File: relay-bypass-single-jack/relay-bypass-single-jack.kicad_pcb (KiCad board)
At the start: 2 copper layers, 59 x 25.8 mm, 62 parts, among them J1 4, J2 8, J3 4, J4 3, K1 IM05JR, Q1 DMN62D0U-7, Q2 DMP3099L, Q3 DMN62D0U-7, U1 STM32C011F4Ux, U3 TLV76701DRVR, U6 TLP170AM

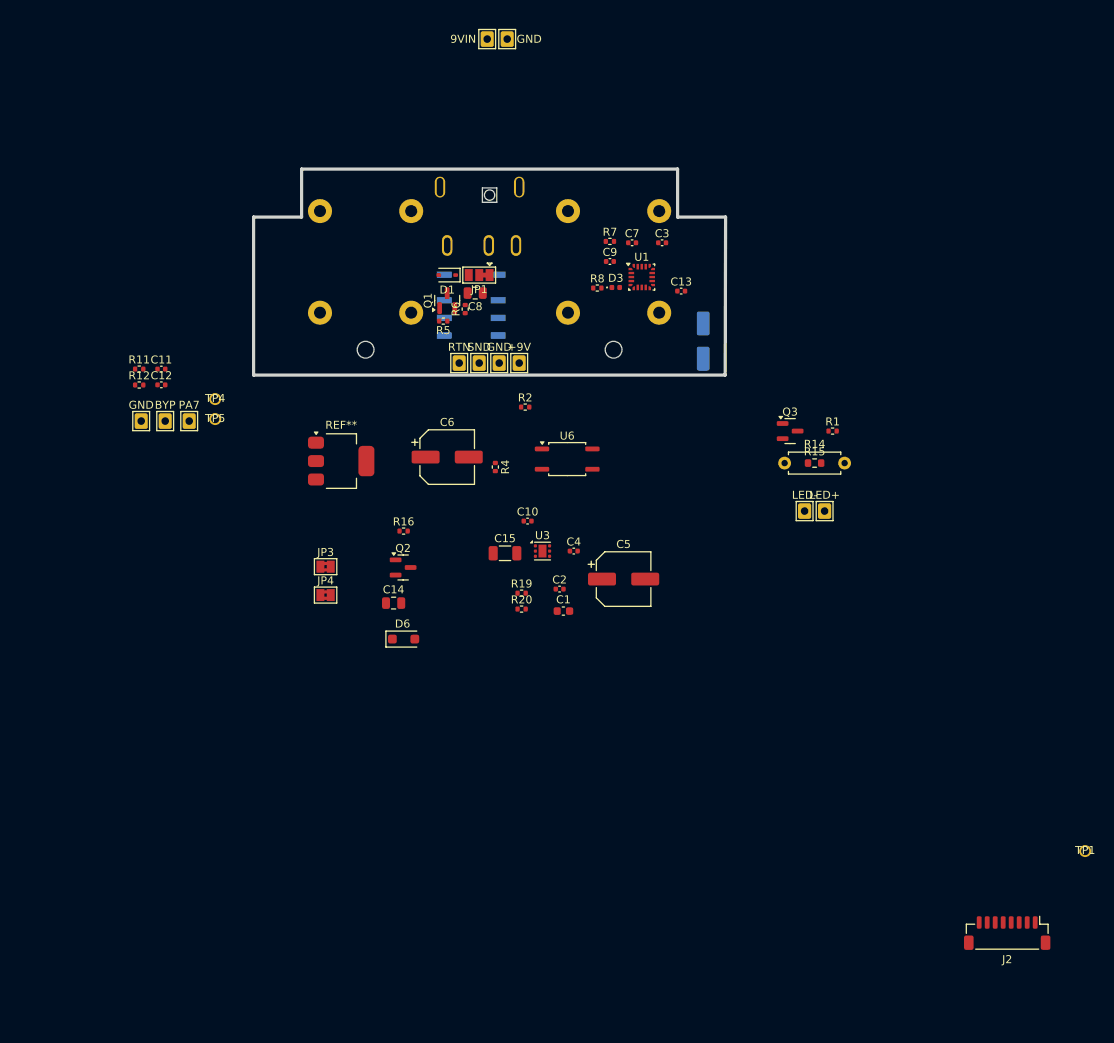
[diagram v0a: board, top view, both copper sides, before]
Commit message: Added second project for exploring a single-jack side mounted version
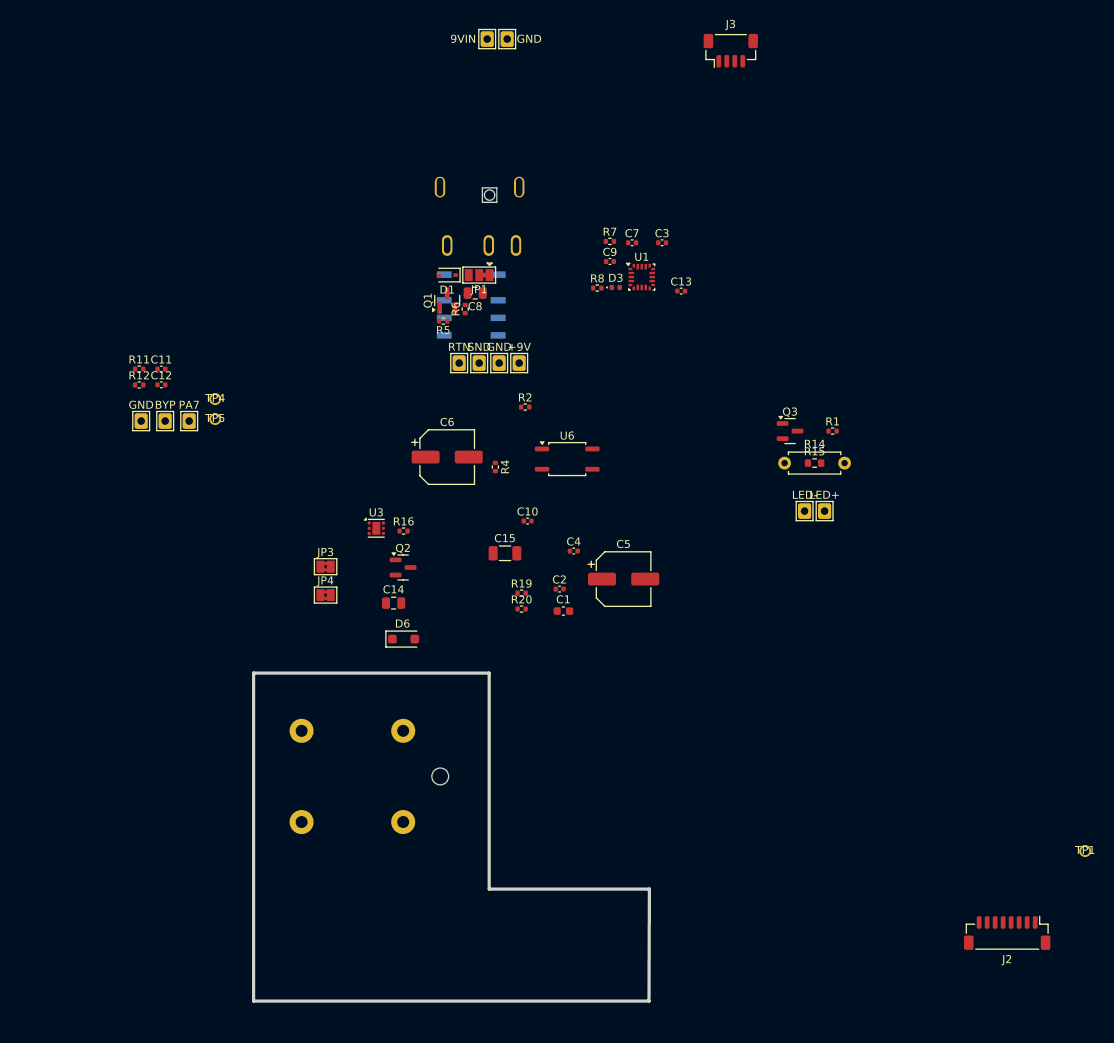
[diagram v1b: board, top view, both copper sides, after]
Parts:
- removed REF**: SOT-223, Package_TO_SOT_SMD:SOT-223
- removed REF**: CP_Elec_5x5.8, Capacitor_SMD:CP_Elec_5x5.8
- J3: footprint g-con:Amphenol_ACJM-MHDR(M) -> Connector_JST:JST_SH_BM04B-SRSS-TB_1x04-1MP_P1.00mm_Vertical; moved to F.Cu
- moved J1 75.9 mm to (72.3, 126.9), turned to 180 degrees
- moved J3 21.5 mm to (130.2, 36.2), turned to 0 degrees
- moved U3 21.0 mm to (85.9, 95.9)
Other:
- board size 59 x 25.8 mm -> 49.5 x 41 mm
- board text added: "TODO add 1590b enclosure dimensions"

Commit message: Pivoted to dual-jack version on opposing sides.
125B only, using "innie" jacks. Solder-in-place.
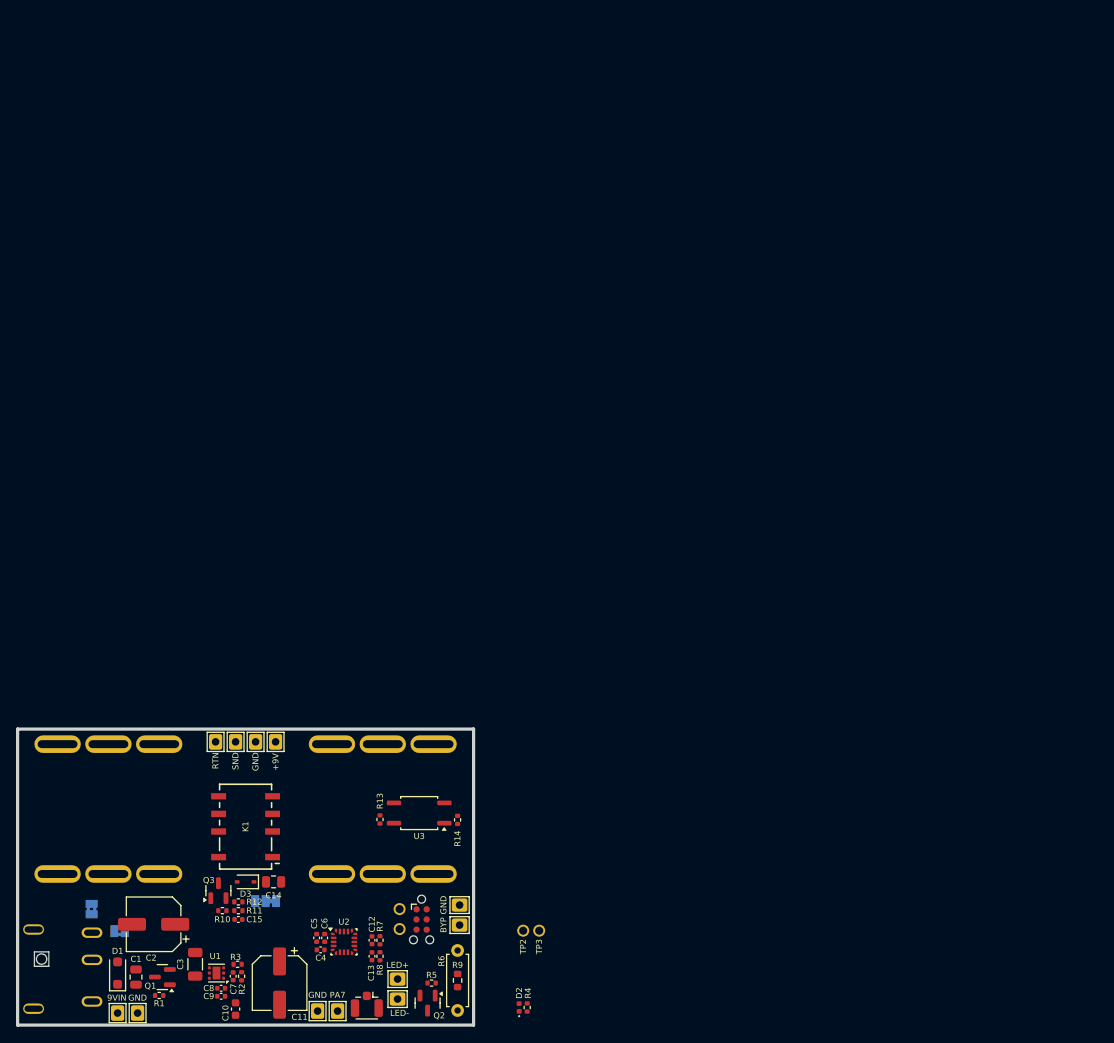
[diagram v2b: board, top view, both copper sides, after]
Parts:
- removed the J1 at (72.3, 126.9)
- removed TP1: PA3, g-art:TestPoint_PTH_H1.02mm_NoOutline
- added J4: AudioJack3_Switch, g-con:Jack_6.35mm_Neutrik_NMJ6HCD2_LARGE_SLOTS, B.Cu at (100.0, 131.0)
- added J5: Conn_Coaxial_Small, Connector_Coaxial:U.FL_Hirose_U.FL-R-SMT-1_Vertical, F.Cu at (84.7, 155.4)
- added REF**: Footswitch_SPST, g-art:Footswitch_SPST, F.Cu at (69.5, 153.5)
- added TP4: TX, g-art:TestPoint_PTH_H1.02mm_NoOutline, F.Cu at (88.8, 146.0)
- added TP5: RX, g-art:TestPoint_PTH_H1.02mm_NoOutline, F.Cu at (88.8, 143.5)
- added WP12: GND, g-art:WirePad_H0.95mm_22-24AWG, F.Cu at (78.5, 156.2)
- J2: value 8 -> TC2030; footprint Connector_JST:JST_SH_BM08B-SRSS-TB_1x08-1MP_P1.00mm_Vertical -> Connector:Tag-Connect_TC2030-IDC-NL_2x03_P1.27mm_Vertical
- J3: value 4 -> AudioJack3_Switch; footprint Connector_JST:JST_SH_BM04B-SRSS-TB_1x04-1MP_P1.00mm_Vertical -> g-con:Jack_6.35mm_Neutrik_NMJ6HCD2_LARGE_SLOTS; moved to B.Cu
- JP1: renamed from JP3; moved to B.Cu
- JP2: renamed from JP4; moved to B.Cu
- JP3: renamed from JP1; moved to B.Cu
- K1: moved to F.Cu
- moved J3 131.5 mm to (39.0, 131.0)
- moved WP1 130.2 mm to (53.5, 156.5)
- moved WP2 130.2 mm to (56.0, 156.5)
- moved J1 108.8 mm to (45.8, 151.0), turned to 180 degrees
- moved C6 96.6 mm to (79.4, 147.1), turned to -90 degrees
- moved R11 95.7 mm to (68.7, 143.7), turned to 180 degrees
- moved C5 95.4 mm to (78.4, 147.1), turned to -90 degrees
- moved C15 94.5 mm to (68.7, 144.8), turned to 180 degrees
- moved C4 93.9 mm to (78.9, 148.6), turned to 180 degrees
- moved U2 91.1 mm to (81.8, 147.6)
- moved D2 90.8 mm to (103.8, 155.8), turned to 90 degrees
- moved R4 90.4 mm to (104.8, 155.8), turned to 90 degrees
- moved R5 85.3 mm to (92.8, 152.8)
- moved Q2 84.6 mm to (92.3, 155.2), turned to -90 degrees
- moved JP3 82.7 mm to (72.0, 142.5)
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- renumbered C14 to C1, C1 to C10, C5 to C11, C11 to C13, C8 to C14, C9 to C15, C6 to C2, C15 to C3, C13 to C4, C7 to C5, C3 to C6, C10 to C7, C4 to C8, C2 to C9, D6 to D1, D3 to D2, D1 to D3, J4 to J1, Q2 to Q1, Q3 to Q2, Q1 to Q3, R16 to R1, R5 to R10, R7 to R11, R6 to R12, R2 to R13, R4 to R14, R20 to R2, R19 to R3, R8 to R4, R1 to R5, R14 to R6, R12 to R7, R11 to R8, R15 to R9, TP5 to TP2, TP4 to TP3, U3 to U1, U1 to U2, U6 to U3, WP5 to WP1, WP13 to WP11, WP6 to WP2, WP7 to WP3, WP8 to WP4, WP9 to WP5, WP3 to WP6, WP1 to WP7, WP11 to WP8, WP12 to WP9
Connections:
- net Net-(K1-Pad6) renamed /Relay_And_Jacks/OUT_R
- net Net-(Q1-S) renamed /Relay_And_Jacks/ISNS_R
- C2 pad 2: GNDA -> GND
- J2 pad 2: /SWCLK -> /SWDIO
- J2 pad 3: GNDD -> /NRST
- J2 pad 4: /SWDIO -> /SWCLK
- J2 pad 5: /NRST -> GNDD
- J2 pad 6: GNDD -> /UART1_TX
- R1 pad 2: GNDA -> GND
- U3 pad 2: (no net) -> GNDD
- U3 pad 3: GNDD -> GNDA
- U3 pad 4: GNDA -> /Relay_And_Jacks/OUT
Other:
- board size 49.5 x 41 mm -> 57 x 37 mm

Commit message: Scratchwork
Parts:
- removed REF**: Footswitch_SPST, g-art:Footswitch_SPST
- added C16: 4.7u, Capacitor_SMD:C_1206_3216Metric, B.Cu at (72.8, 156.3)
- added C17: 100n, Capacitor_SMD:C_0402_1005Metric, B.Cu at (71.5, 152.0)
- added U4: LM317LCPK, Package_TO_SOT_SMD:SOT-223, B.Cu at (66.5, 151.5)
- C10: footprint Capacitor_SMD:C_0603_1608Metric -> Capacitor_SMD:C_0805_2012Metric
- C11: value 47u -> 100n; footprint Capacitor_SMD:CP_Elec_6.3x5.8 -> Capacitor_SMD:C_0402_1005Metric
- moved TP2 29.7 mm to (74.8, 150.7)
- moved TP3 29.7 mm to (76.8, 150.7)
- moved R4 23.3 mm to (81.8, 151.5), turned to 180 degrees
- moved D2 22.1 mm to (81.8, 152.5), turned to 180 degrees
- moved C11 9.37 mm to (64.5, 152.2), turned to 90 degrees
- moved C10 4.34 mm to (72.2, 154.2), turned to 0 degrees
- moved C3 2.21 mm to (62.5, 152.5), turned to -90 degrees
- moved C9 1.15 mm to (66.8, 155.5)
- moved C8 1.06 mm to (66.8, 154.4)
- moved U1 0.73 mm to (66.5, 152.0)
- moved C7 0.64 mm to (68.4, 152.4)
- moved R2 0.64 mm to (69.5, 152.4)
- moved R3 0.64 mm to (69.0, 150.9)
- moved C5 0.52 mm to (78.0, 147.3)
- moved C4 0.22 mm to (78.8, 148.8)
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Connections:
- C11 pad 1: +3.3V -> +9V
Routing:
- net /Relay_And_Jacks/IN: track 0.00 -> 26.7 mm
- net /MUTE: track 0.00 -> 25.8 mm
- net /RLY_SET: track 0.00 -> 22.6 mm, vias 0 -> 2
- net /FB: track 0.00 -> 20.8 mm, vias 0 -> 1
- net /ISNS: track 0.00 -> 20.6 mm
- net /UART1_TX: track 0.00 -> 20.3 mm, vias 0 -> 2
- net /Relay_And_Jacks/OUT_R: track 0.00 -> 20.3 mm, vias 0 -> 2
- net /NRST: track 0.00 -> 19.7 mm, vias 0 -> 2
- net /Relay_And_Jacks/SEND: track 0.00 -> 17.6 mm
- net /SWCLK: track 0.00 -> 15.9 mm, vias 0 -> 2
- net /SWDIO: track 0.00 -> 15.6 mm, vias 0 -> 2
- net /Relay_And_Jacks/OUT: track 0.00 -> 14.1 mm
- net GNDD: track 0.00 -> 14.0 mm, vias 0 -> 9
- net /LED_EXT: track 0.00 -> 12.9 mm
- net +9VIN: track 0.00 -> 12.0 mm
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- added copper zone on B.Cu, net +3.3V
- added copper zone on F.Cu, net +3.3V
- added copper zone on In2.Cu, net +3.3V
- added copper zone on F.Cu, net +9V
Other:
- copper layers 2 -> 4
